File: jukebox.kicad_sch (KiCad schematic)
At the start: 34 parts, among them J1 USB_B_Micro, J2 Conn_01x19_Pin, J3 Conn_01x19_Pin, Q1 SS8050, Q2 SS8050, SW1 SW_Push, SW2 SW_Push, U1 CP2102N-Axx-xQFN28, U2 AMS1117-3.3

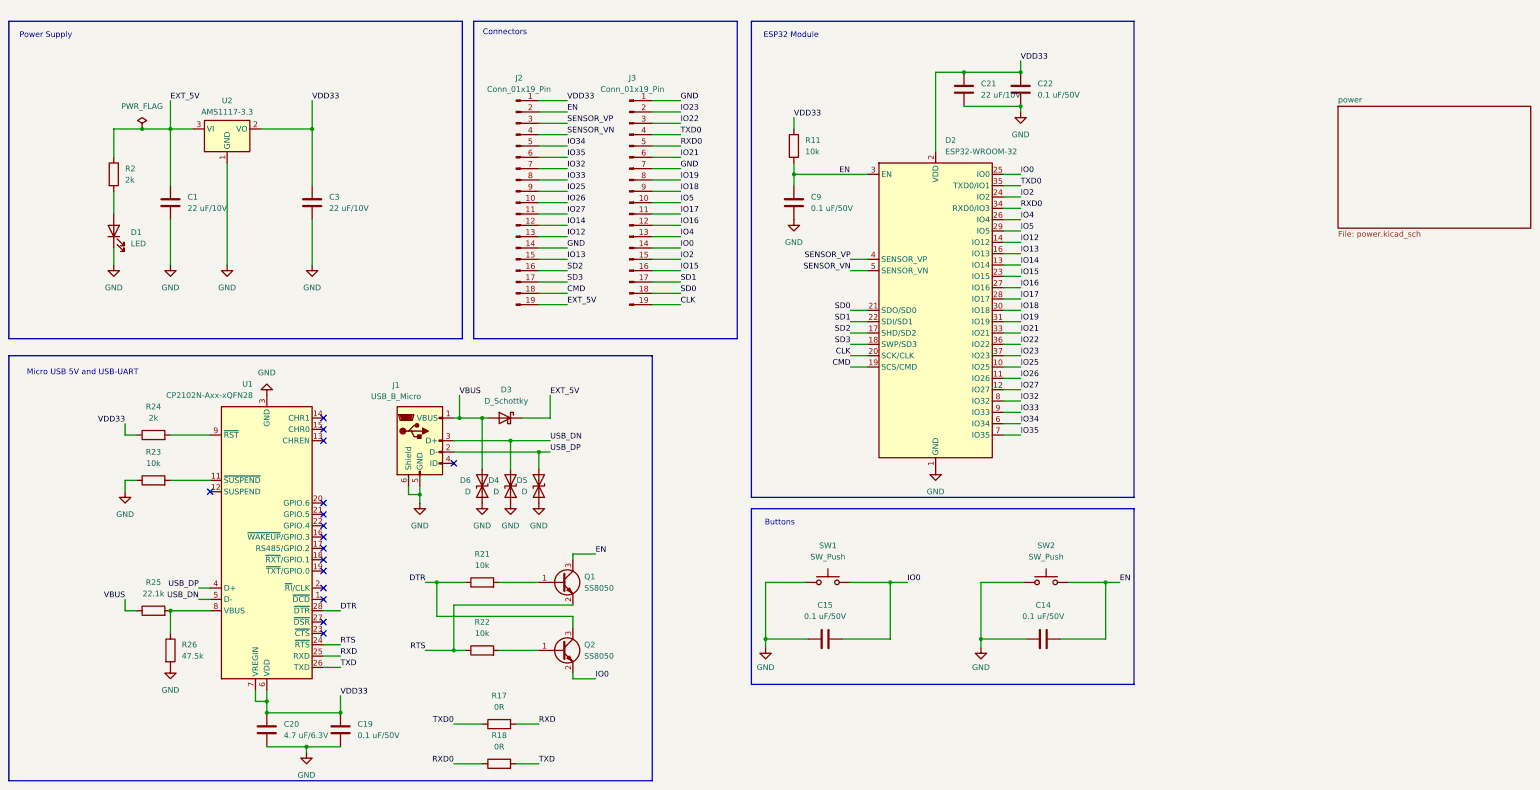
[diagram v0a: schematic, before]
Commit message: power and sd added
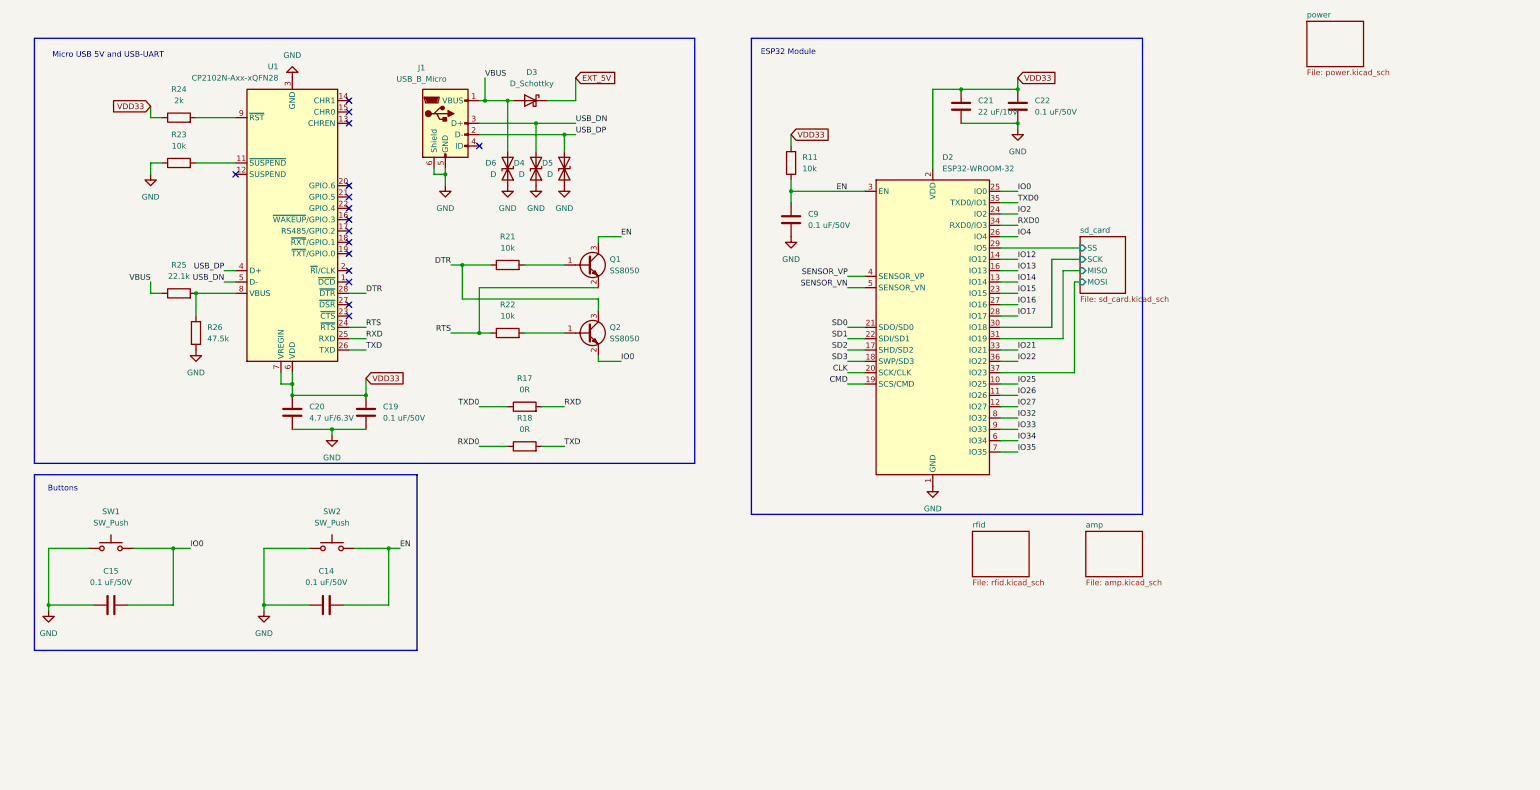
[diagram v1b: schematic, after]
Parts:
- removed C1, C3: 22 uF/10V, Capacitor_SMD:C_0603_1608Metric, symbol Device:C
- removed D1: LED, LED_SMD:LED_0603_1608Metric, symbol Device:LED
- removed J2, J3: Conn_01x19_Pin, Connector_PinHeader_2.54mm:PinHeader_1x19_P2.54mm_Vertical, symbol Connector:Conn_01x19_Pin
- removed R2: 2k, Resistor_SMD:R_0402_1005Metric, symbol Device:R
- removed U2: AMS1117-3.3, Package_TO_SOT_SMD:SOT-223-3_TabPin2, symbol Regulator_Linear:AMS1117-3.3
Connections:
- net IO18 renamed sd_card/SCK
- net IO19 renamed sd_card/MISO
- net IO23 renamed sd_card/MOSI
- net IO5 renamed sd_card/SS
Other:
- added sheet amp (amp.kicad_sch)
- added sheet rfid (rfid.kicad_sch)
- added sheet sd_card (sd_card.kicad_sch)
- note removed: "Connectors"
- note removed: "Power Supply"
- moved on the sheet: C14, C15, C19, C20, C21, C22, C9, D2, D3, D4, D5, D6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

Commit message: amp and sd sheets revision 1
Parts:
- added C10, C11: 22 uF/10V, Capacitor_SMD:C_0603_1608Metric, symbol Device:C
- added D1: LED, LED_SMD:LED_0603_1608Metric, symbol Device:LED
- added R7: 2k, Resistor_SMD:R_0402_1005Metric, symbol Device:R
- added U4: AMS1117-3.3, Package_TO_SOT_SMD:SOT-223-3_TabPin2, symbol Regulator_Linear:AMS1117-3.3
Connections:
- net EXT_5V: now also C10.1, R7.1, U4.3 (VI)
- net GND: now also C10.2, C11.2, D1.1 (K), U4.1 (GND)
- net VDD33: now also C11.1, U4.2 (VO)
- net IO22 renamed amp/DIN
- net IO25 renamed amp/LRCLK
- net IO26 renamed amp/BCLK
- new net: D1.2 (A), R7.2
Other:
- removed sheet power
- sheet amp ports: added BCLK, DIN, LRCLK; removed none
- note added: "Power Supply"
- moved on the sheet: C21, C22, C9, D2, R11

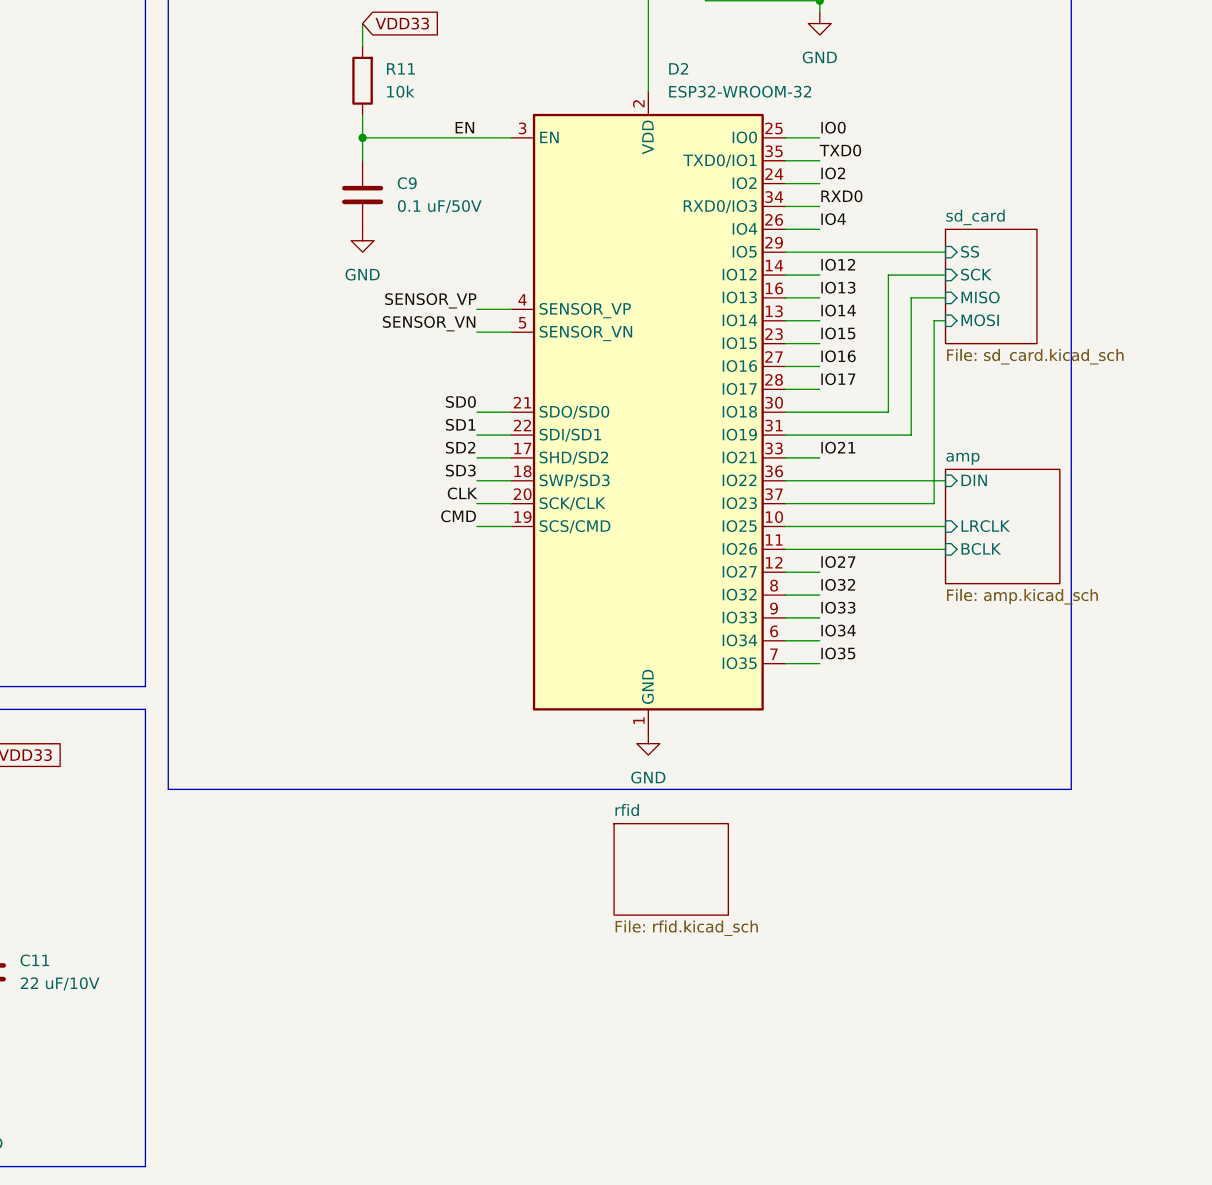
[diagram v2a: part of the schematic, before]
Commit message: rfid revision 1 sch
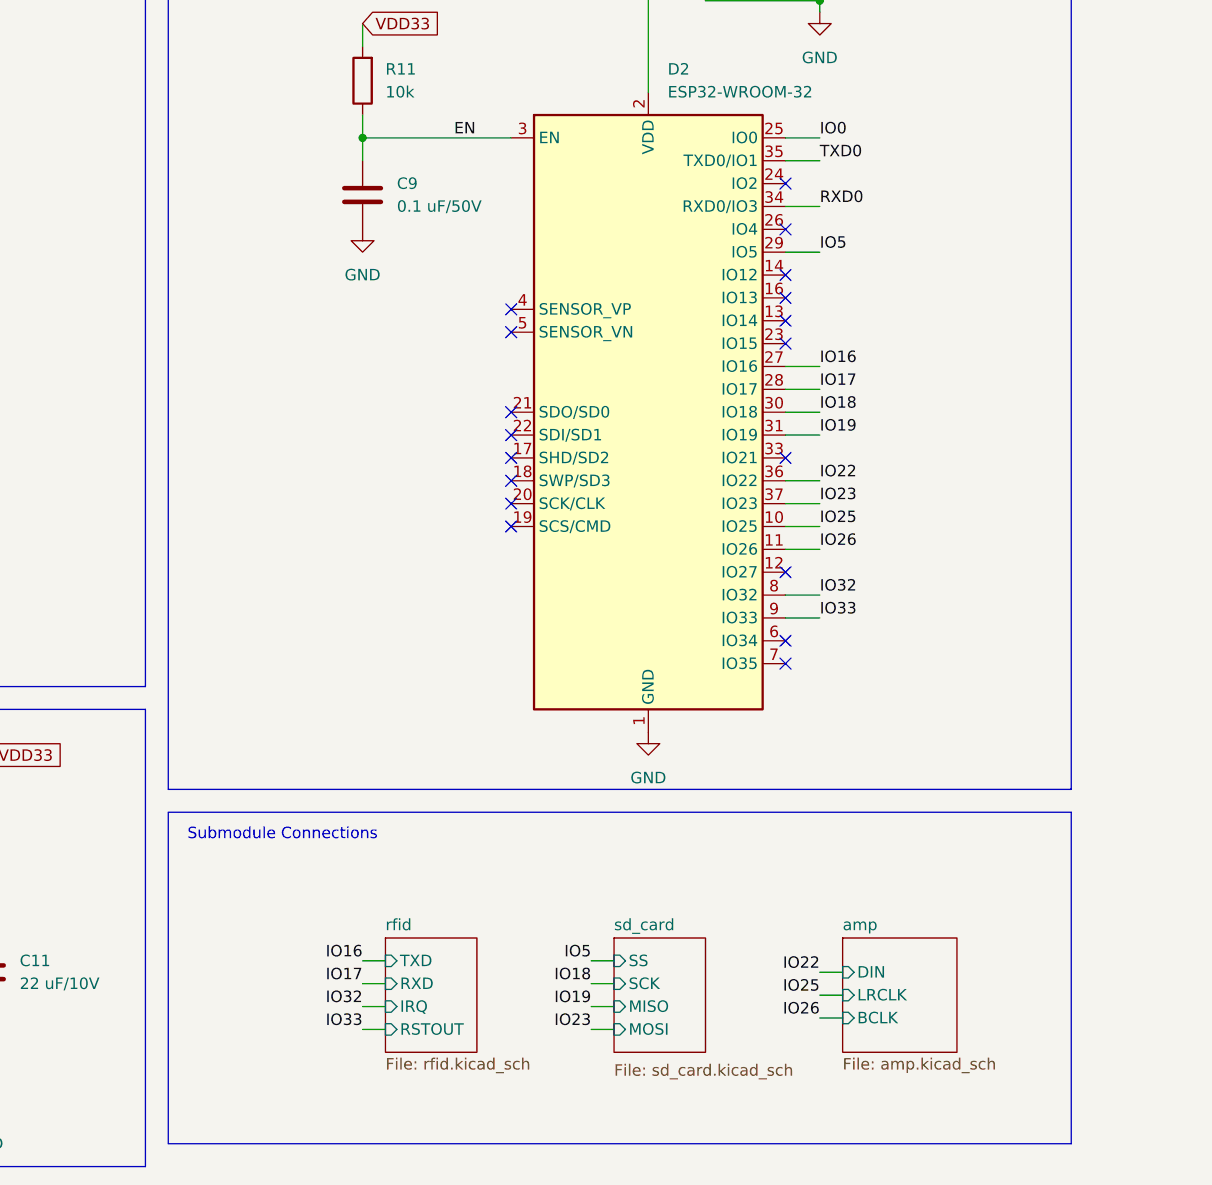
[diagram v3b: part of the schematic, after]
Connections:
- net CLK: no longer names the net of D2.20 (SCK/CLK)
- net CMD: no longer names the net of D2.19 (SCS/CMD)
- net IO12: no longer names the net of D2.14 (IO12)
- net IO13: no longer names the net of D2.16 (IO13)
- net IO14: no longer names the net of D2.13 (IO14)
- net IO15: no longer names the net of D2.23 (IO15)
- net IO2: no longer names the net of D2.24 (IO2)
- net IO21: no longer names the net of D2.33 (IO21)
- net IO27: no longer names the net of D2.12 (IO27)
- net IO34: no longer names the net of D2.6 (IO34)
- net IO35: no longer names the net of D2.7 (IO35)
- net IO4: no longer names the net of D2.26 (IO4)
- net SD0: no longer names the net of D2.21 (SDO/SD0)
- net SD1: no longer names the net of D2.22 (SDI/SD1)
- net SD2: no longer names the net of D2.17 (SHD/SD2)
- net SD3: no longer names the net of D2.18 (SWP/SD3)
- net SENSOR_VN: no longer names the net of D2.5 (SENSOR_VN)
- net SENSOR_VP: no longer names the net of D2.4 (SENSOR_VP)
- net amp/BCLK renamed IO26
- net amp/DIN renamed IO22
- net amp/LRCLK renamed IO25
- net sd_card/MISO renamed IO19
- net sd_card/MOSI renamed IO23
- net sd_card/SCK renamed IO18
- net sd_card/SS renamed IO5
- no-connect marks 16 -> 34
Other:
- sheet rfid ports: added IRQ, RSTOUT, RXD, TXD; removed none
- note added: "Submodule Connections"
